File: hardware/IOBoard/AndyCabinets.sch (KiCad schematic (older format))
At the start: 47 parts, among them SW1 Mode_Encoder, SW2 Color_Encoder, U1 74HC14

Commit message: Added faceplate boards
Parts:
- RV1, RV2: footprint Potentiometer_THT:Potentiometer_TT_P0915N -> YonaFootprints:Potentiometer_TT_P0915N_Flush
- U1: footprint (none) -> Package_SO:SOIC-14_3.9x8.7mm_P1.27mm
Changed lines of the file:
@@
 F 0 "RV2" H 3230 3154 50  0000 R CNN
 F 1 "Bright_Pot" H 3230 3245 50  0000 R CNN
-F 2 "Potentiometer_THT:Potentiometer_TT_P0915N" H 3300 3200 50  0001 C CNN
+F 2 "YonaFootprints:Potentiometer_TT_P0915N_Flush" H 3300 3200 50  0001 C CNN
 F 3 "~" H 3300 3200 50  0001 C CNN
 	1    3300 3200
@@
 F 0 "RV1" H 1880 3154 50  0000 R CNN
 F 1 "Speed_Pot" H 1880 3245 50  0000 R CNN
-F 2 "Potentiometer_THT:Potentiometer_TT_P0915N" H 1950 3200 50  0001 C CNN
+F 2 "YonaFootprints:Potentiometer_TT_P0915N_Flush" H 1950 3200 50  0001 C CNN
 F 3 "~" H 1950 3200 50  0001 C CNN
 	1    1950 3200
@@
 F 0 "U1" H 11380 2746 50  0000 L CNN
 F 1 "74HC14" H 11380 2655 50  0000 L CNN
-F 2 "" H 11150 2700 50  0001 C CNN
+F 2 "Package_SO:SOIC-14_3.9x8.7mm_P1.27mm" H 11150 2700 50  0001 C CNN
 F 3 "http://www.ti.com/lit/gpn/sn74HC14" H 11150 2700 50  0001 C CNN
 	7    11150 2700

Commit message: After PCB v2
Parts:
- removed C9: 1uF, Capacitor_SMD:C_0805_2012Metric, symbol Device:C
- C11, C13: value 0.01uF -> 0.1uF
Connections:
- net GPIO32_MODE_BTN: now also U1.12; no longer U1.13
- net GPIO33_MODE_B: now also U1.4; no longer U1.3
- net at C7.1, R7.2: now also U1.3; no longer U1.4
- net at C13.1, R12.1: now also U1.13; no longer U1.12
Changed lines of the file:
@@
-$EndComp
-$Comp
-L power:GNDD #PWR015
-U 1 1 5E283166
-P 6050 3450
-F 0 "#PWR015" H 6050 3200 50  0001 C CNN
-F 1 "GNDD" H 6054 3295 50  0000 C CNN
-F 2 "" H 6050 3450 50  0001 C CNN
-F 3 "" H 6050 3450 50  0001 C CNN
-	1    6050 3450
-	1    0    0    -1
-$EndComp
-$Comp
-L Device:C C9
-U 1 1 5E28316C
-P 6050 3300
-F 0 "C9" H 6165 3346 50  0000 L CNN
-F 1 "1uF" H 6165 3255 50  0000 L CNN
-F 2 "Capacitor_SMD:C_0805_2012Metric" H 6088 3150 50  0001 C CNN
-F 3 "~" H 6050 3300 50  0001 C CNN
-	1    6050 3300
-	1    0    0    -1
-$EndComp
-$Comp
-L AndyCabinets-rescue:+3.3V-ESP32-PoE-ISO_Rev_C #PWR013
-U 1 1 5E28E6C3
-P 6050 3150
-F 0 "#PWR013" H 6050 3000 50  0001 C CNN
-F 1 "+3.3V" H 6065 3278 50  0000 L CNN
-F 2 "" H 6050 3150 60  0000 C CNN
-F 3 "" H 6050 3150 60  0000 C CNN
-	1    6050 3150
-	1    0    0    -1
 $EndComp
 $Comp
@@
 P 8800 2900
 F 0 "C11" H 8915 2946 50  0000 L CNN
-F 1 "0.01uF" H 8915 2855 50  0000 L CNN
+F 1 "0.1uF" H 8915 2855 50  0000 L CNN
 F 2 "Capacitor_SMD:C_0402_1005Metric" H 8838 2750 50  0001 C CNN
 F 3 "~" H 8800 2900 50  0001 C CNN
@@
 $EndComp
 $Comp
-L Device:R R11
-U 1 1 5E44CEB9
-P 8300 5500
-F 0 "R11" H 8150 5550 50  0000 L CNN
-F 1 "10K" H 8100 5450 50  0000 L CNN
-F 2 "Resistor_SMD:R_0402_1005Metric" V 8230 5500 50  0001 C CNN
-F 3 "~" H 8300 5500 50  0001 C CNN
-	1    8300 5500
-	1    0    0    -1
-$EndComp
-$Comp
 L Device:C C13
 U 1 1 5E44CEBF
 P 8800 5800
 F 0 "C13" H 8915 5846 50  0000 L CNN
-F 1 "0.01uF" H 8915 5755 50  0000 L CNN
+F 1 "0.1uF" H 8915 5755 50  0000 L CNN
 F 2 "Capacitor_SMD:C_0402_1005Metric" H 8838 5650 50  0001 C CNN
 F 3 "~" H 8800 5800 50  0001 C CNN
@@
 F 3 "http://www.ti.com/lit/gpn/sn74HC14" H 5750 4800 50  0001 C CNN
 	2    5750 4800
-	1    0    0    -1
+	-1   0    0    1
 $EndComp
 $Comp
@@
 F 3 "http://www.ti.com/lit/gpn/sn74HC14" H 9350 5650 50  0001 C CNN
 	6    9350 5650
-	-1   0    0    1
+	1    0    0    -1
 $EndComp
 Wire Wire Line
@@
 	1    0    0    -1
 $EndComp
+$Comp
+L Device:R R11
+U 1 1 5E44CEB9
+P 8300 5500
+F 0 "R11" H 8100 5550 50  0000 L CNN
+F 1 "10K" H 8100 5450 50  0000 L CNN
+F 2 "Resistor_SMD:R_0402_1005Metric" V 8230 5500 50  0001 C CNN
+F 3 "~" H 8300 5500 50  0001 C CNN
+	1    8300 5500
+	1    0    0    -1
+$EndComp

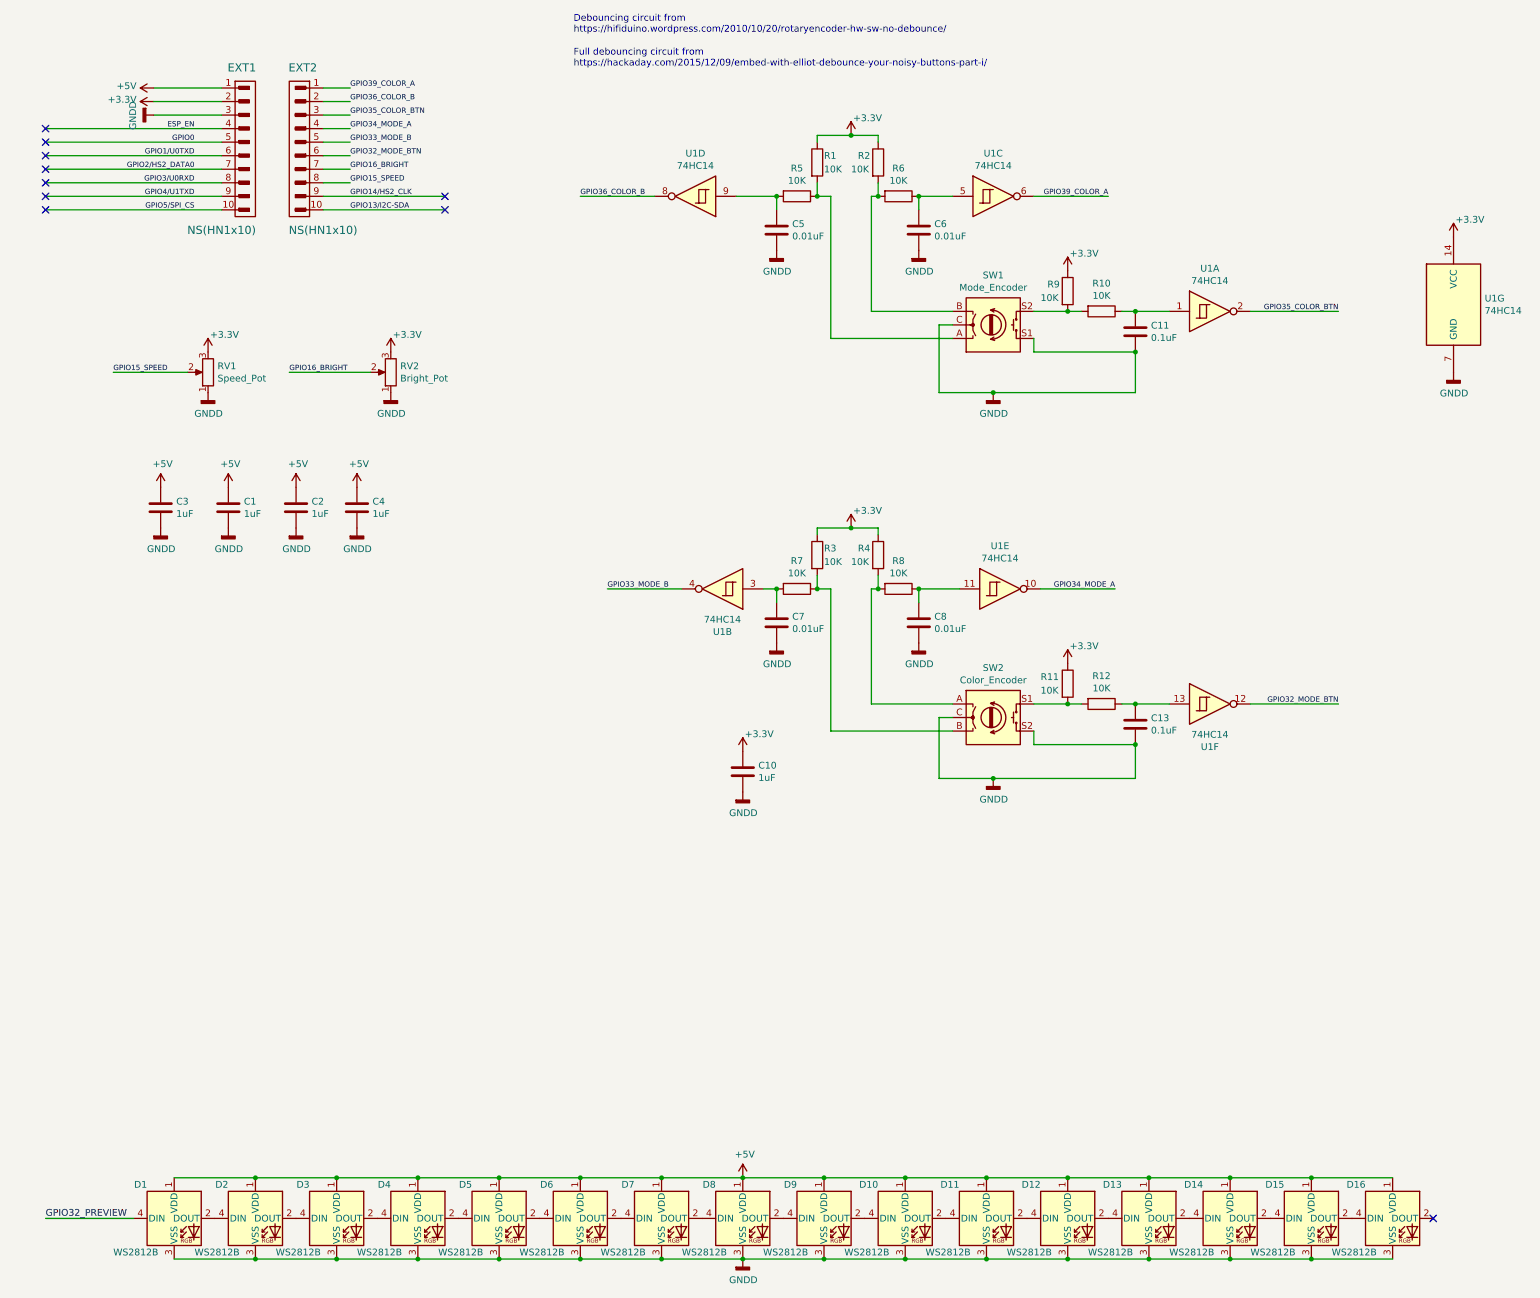
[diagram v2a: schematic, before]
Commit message: Initial working remote version; some minor PCB changes
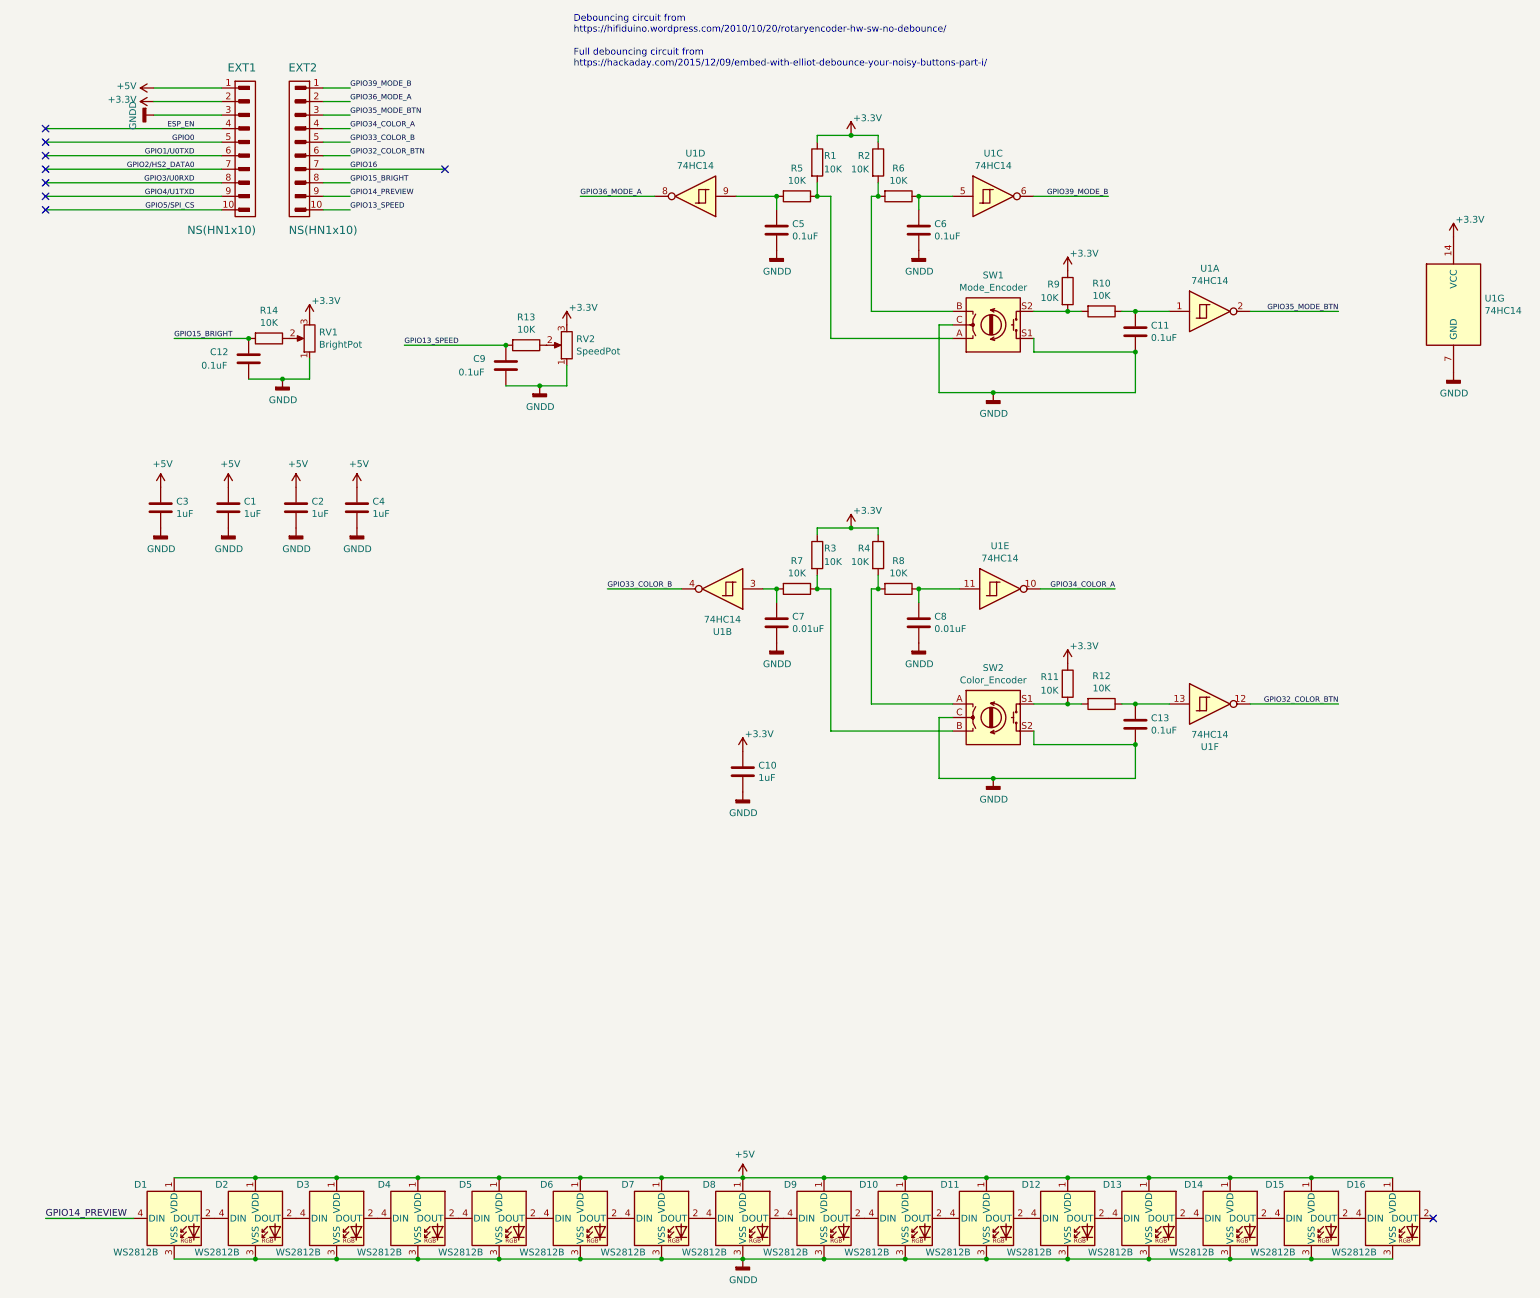
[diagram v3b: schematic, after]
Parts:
- added C12, C9: 0.1uF, Capacitor_SMD:C_0402_1005Metric, symbol Device:C
- added R13, R14: 10K, Resistor_SMD:R_0402_1005Metric, symbol Device:R
- C5, C6: value 0.01uF -> 0.1uF
- RV1: value Speed_Pot -> BrightPot
- RV2: value Bright_Pot -> SpeedPot
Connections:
- net GPIO32_PREVIEW is gone; now on net GPIO14_PREVIEW: D1.4 (DIN)
- net GNDD: now also C12.2, C9.2
- net GPIO13/I2C-SDA renamed GPIO13_SPEED
- net GPIO13_SPEED: now also C9.1, R13.2
- net GPIO14/HS2_CLK renamed GPIO14_PREVIEW
- net GPIO15_SPEED: no longer names the net of RV1.2
- net GPIO15_SPEED: now also R14.1; no longer EXT2.8
- net GPIO16_BRIGHT: no longer names the net of RV2.2
- net GPIO16_BRIGHT: now also R13.1; no longer EXT2.7
- net GPIO32_MODE_BTN renamed GPIO32_COLOR_BTN
- net GPIO33_MODE_B renamed GPIO33_COLOR_B
- net GPIO34_MODE_A renamed GPIO34_COLOR_A
- net GPIO35_COLOR_BTN renamed GPIO35_MODE_BTN
- net GPIO36_COLOR_B renamed GPIO36_MODE_A
- net GPIO39_COLOR_A renamed GPIO39_MODE_B
- new net GPIO15_BRIGHT: C12.1, EXT2.8, R14.2
- new net GPIO16: EXT2.7
- no-connect marks 10 -> 9
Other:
- moved on the sheet: RV1, RV2
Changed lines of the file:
@@
 L Device:R_POT RV2
 U 1 1 5DB1EC9A
-P 3300 3200
-F 0 "RV2" H 3230 3154 50  0000 R CNN
-F 1 "Bright_Pot" H 3230 3245 50  0000 R CNN
-F 2 "YonaFootprints:Potentiometer_TT_P0915N_Flush" H 3300 3200 50  0001 C CNN
-F 3 "~" H 3300 3200 50  0001 C CNN
-	1    3300 3200
+P 4600 3000
+F 0 "RV2" H 4530 2954 50  0000 R CNN
+F 1 "SpeedPot" H 4530 3045 50  0000 R CNN
+F 2 "YonaFootprints:Potentiometer_TT_P0915N_Flush" H 4600 3000 50  0001 C CNN
+F 3 "~" H 4600 3000 50  0001 C CNN
+	1    4600 3000
 	-1   0    0    1
 $EndComp
@@
 L power:GNDD #PWR0104
 U 1 1 5DB22F79
-P 3300 3350
-F 0 "#PWR0104" H 3300 3100 50  0001 C CNN
-F 1 "GNDD" H 3304 3195 50  0000 C CNN
-F 2 "" H 3300 3350 50  0001 C CNN
-F 3 "" H 3300 3350 50  0001 C CNN
-	1    3300 3350
+P 4400 3300
+F 0 "#PWR0104" H 4400 3050 50  0001 C CNN
+F 1 "GNDD" H 4404 3145 50  0000 C CNN
+F 2 "" H 4400 3300 50  0001 C CNN
+F 3 "" H 4400 3300 50  0001 C CNN
+	1    4400 3300
 	1    0    0    -1
 $EndComp
@@
 L Device:R_POT RV1
 U 1 1 5DB2A214
-P 1950 3200
-F 0 "RV1" H 1880 3154 50  0000 R CNN
-F 1 "Speed_Pot" H 1880 3245 50  0000 R CNN
-F 2 "YonaFootprints:Potentiometer_TT_P0915N_Flush" H 1950 3200 50  0001 C CNN
-F 3 "~" H 1950 3200 50  0001 C CNN
-	1    1950 3200
+P 2700 2950
+F 0 "RV1" H 2630 2904 50  0000 R CNN
+F 1 "BrightPot" H 2630 2995 50  0000 R CNN
+F 2 "YonaFootprints:Potentiometer_TT_P0915N_Flush" H 2700 2950 50  0001 C CNN
+F 3 "~" H 2700 2950 50  0001 C CNN
+	1    2700 2950
 	-1   0    0    1
-$EndComp
-$Comp
-L power:GNDD #PWR0106
-U 1 1 5DB2A21A
-P 1950 3350
-F 0 "#PWR0106" H 1950 3100 50  0001 C CNN
-F 1 "GNDD" H 1954 3195 50  0000 C CNN
-F 2 "" H 1950 3350 50  0001 C CNN
-F 3 "" H 1950 3350 50  0001 C CNN
-	1    1950 3350
-	1    0    0    -1
 $EndComp
 $Comp
@@
 $EndComp
 Text Label 750  9450 0    50   ~ 0
-GPIO32_PREVIEW
+GPIO14_PREVIEW
 $Comp
 L LED:WS2812B D2
@@
 Text Label 1850 2000 2    39   ~ 0
 GPIO5/SPI_CS
-Text Label 3000 2000 0    39   ~ 0
-GPIO13/I2C-SDA
 Text Label 3000 1900 0    39   ~ 0
-GPIO14/HS2_CLK
+GPIO14_PREVIEW
 Text Label 3000 1800 0    39   ~ 0
-GPIO15_SPEED
+GPIO15_BRIGHT
 Text Label 3000 1700 0    39   ~ 0
-GPIO16_BRIGHT
+GPIO16
 Text Label 3000 1500 0    39   ~ 0
-GPIO33_MODE_B
+GPIO33_COLOR_B
 Text Label 3000 1400 0    39   ~ 0
-GPIO34_MODE_A
+GPIO34_COLOR_A
 Text Label 3000 1200 0    39   ~ 0
-GPIO36_COLOR_B
+GPIO36_MODE_A
 Text Label 3000 1100 0    39   ~ 0
-GPIO39_COLOR_A
+GPIO39_MODE_B
 $Comp
 L AndyCabinets-rescue:+5V-ESP32-PoE-ISO_Rev_C #PWR0108
@@
 	2050 2000 750  2000
 Wire Wire Line
-	3700 2000 2800 2000
-Wire Wire Line
-	2800 1900 3700 1900
-Wire Wire Line
 	2050 1300 1550 1300
 Wire Wire Line
@@
 	1    0    0    -1
 $EndComp
-NoConn ~ 3700 2000
-NoConn ~ 3700 1900
 NoConn ~ 750  2000
 NoConn ~ 750  1900
@@
 L AndyCabinets-rescue:+3.3V-ESP32-PoE-ISO_Rev_C #PWR0101
 U 1 1 5E0E7FA8
-P 3300 3050
-F 0 "#PWR0101" H 3300 2900 50  0001 C CNN
-F 1 "+3.3V" H 3315 3178 50  0000 L CNN
-F 2 "" H 3300 3050 60  0000 C CNN
-F 3 "" H 3300 3050 60  0000 C CNN
-	1    3300 3050
+P 4600 2850
+F 0 "#PWR0101" H 4600 2700 50  0001 C CNN
+F 1 "+3.3V" H 4615 2978 50  0000 L CNN
+F 2 "" H 4600 2850 60  0000 C CNN
+F 3 "" H 4600 2850 60  0000 C CNN
+	1    4600 2850
 	1    0    0    -1
 $EndComp
@@
 L AndyCabinets-rescue:+3.3V-ESP32-PoE-ISO_Rev_C #PWR0105
 U 1 1 5E0F28C5
-P 1950 3050
-F 0 "#PWR0105" H 1950 2900 50  0001 C CNN
-F 1 "+3.3V" H 1965 3178 50  0000 L CNN
-F 2 "" H 1950 3050 60  0000 C CNN
-F 3 "" H 1950 3050 60  0000 C CNN
-	1    1950 3050
-	1    0    0    -1
-$EndComp
-Wire Wire Line
-	1250 3200 1800 3200
+P 2700 2800
+F 0 "#PWR0105" H 2700 2650 50  0001 C CNN
+F 1 "+3.3V" H 2715 2928 50  0000 L CNN
+F 2 "" H 2700 2800 60  0000 C CNN
+F 3 "" H 2700 2800 60  0000 C CNN
+	1    2700 2800
+	1    0    0    -1
+$EndComp
+Wire Wire Line
+	1700 2950 2250 2950
 Wire Wire Line
 	750  9450 1400 9450
 Wire Wire Line
-	2550 3200 3150 3200
-Wire Wire Line
 	3000 1100 2800 1100
 Wire Wire Line
@@
 	3000 1200 2800 1200
 Wire Wire Line
-	3000 1700 2800 1700
-Wire Wire Line
 	2800 1800 3000 1800
-Text Label 1250 3200 0    39   ~ 0
-GPIO15_SPEED
-Text Label 2550 3200 0    39   ~ 0
-GPIO16_BRIGHT
-Text Label 8600 1900 2    39   ~ 0
-GPIO39_COLOR_A
-Text Label 4700 1900 0    39   ~ 0
-GPIO36_COLOR_B
+Text Label 1700 2950 0    39   ~ 0
+GPIO15_BRIGHT
+Text Label 3400 3000 0    39   ~ 0
+GPIO13_SPEED
 $Comp
 L Device:C C1
@@
 $EndComp
 $Comp
-L Device:C C5
-U 1 1 5E1C5F20
-P 6150 2150
-F 0 "C5" H 6265 2196 50  0000 L CNN
-F 1 "0.01uF" H 6265 2105 50  0000 L CNN
-F 2 "Capacitor_SMD:C_0402_1005Metric" H 6188 2000 50  0001 C CNN
-F 3 "~" H 6150 2150 50  0001 C CNN
-	1    6150 2150
-	1    0    0    -1
-$EndComp
-$Comp
 L power:GNDD #PWR0102
 U 1 1 5E1C6A2D
@@
 P 7200 2150
 F 0 "C6" H 7315 2196 50  0000 L CNN
-F 1 "0.01uF" H 7315 2105 50  0000 L CNN
+F 1 "0.1uF" H 7315 2105 50  0000 L CNN
 F 2 "Capacitor_SMD:C_0402_1005Metric" H 7238 2000 50  0001 C CNN
 F 3 "~" H 7200 2150 50  0001 C CNN
@@
 $EndComp
 Text Label 8650 4800 2    39   ~ 0
-GPIO34_MODE_A
+GPIO34_COLOR_A
 Text Notes 4650 700  0    50   ~ 0
 Debouncing circuit from \nhttps://hifiduino.wordpress.com/2010/10/20/rotaryencoder-hw-sw-no-debounce/
@@
 	3000 1300 2800 1300
 Text Label 3000 1600 0    39   ~ 0
-GPIO32_MODE_BTN
+GPIO32_COLOR_BTN
 Text Label 3000 1300 0    39   ~ 0
-GPIO35_COLOR_BTN
+GPIO35_MODE_BTN
 $Comp
 L power:+5V #PWR04
@@
 	7450 5750 7350 5750
 Text Label 10300 2750 2    39   ~ 0
-GPIO35_COLOR_BTN
+GPIO35_MODE_BTN
 Text Label 10300 5650 2    39   ~ 0
-GPIO32_MODE_BTN
+GPIO32_COLOR_BTN
 $Comp
 L power:GNDD #PWR0103
@@
 Connection ~ 8800 3050
 Text Label 4900 4800 0    39   ~ 0
-GPIO33_MODE_B
+GPIO33_COLOR_B
 $Comp
 L 74xx:74HC14 U1
@@
 $Comp
 L 74xx:74HC14 U1
-U 3 1 5E46D9F8
-P 7750 1900
-F 0 "U1" H 7750 2217 50  0000 C CNN
-F 1 "74HC14" H 7750 2126 50  0000 C CNN
-F 2 "Package_SO:SOIC-14_3.9x8.7mm_P1.27mm" H 7750 1900 50  0001 C CNN
-F 3 "http://www.ti.com/lit/gpn/sn74HC14" H 7750 1900 50  0001 C CNN
-	3    7750 1900
-	1    0    0    -1
-$EndComp
-$Comp
-L 74xx:74HC14 U1
 U 4 1 5E46F5E2
 P 5550 1900
@@
 	1    0    0    -1
 $EndComp
+$Comp
+L 74xx:74HC14 U1
+U 3 1 5E46D9F8
+P 7750 1900
+F 0 "U1" H 7750 2217 50  0000 C CNN
+F 1 "74HC14" H 7750 2126 50  0000 C CNN
+F 2 "Package_SO:SOIC-14_3.9x8.7mm_P1.27mm" H 7750 1900 50  0001 C CNN
+F 3 "http://www.ti.com/lit/gpn/sn74HC14" H 7750 1900 50  0001 C CNN
+	3    7750 1900
+	1    0    0    -1
+$EndComp
+$Comp
+L Device:R R13
+U 1 1 5E210549
+P 4300 3000
+F 0 "R13" V 4093 3000 50  0000 C CNN
+F 1 "10K" V 4184 3000 50  0000 C CNN
+F 2 "Resistor_SMD:R_0402_1005Metric" V 4230 3000 50  0001 C CNN
+F 3 "~" H 4300 3000 50  0001 C CNN
+	1    4300 3000
+	0    1    1    0
+$EndComp
+$Comp
+L Device:C C5
+U 1 1 5E1C5F20
+P 6150 2150
+F 0 "C5" H 6265 2196 50  0000 L CNN
+F 1 "0.1uF" H 6265 2105 50  0000 L CNN
+F 2 "Capacitor_SMD:C_0402_1005Metric" H 6188 2000 50  0001 C CNN
+F 3 "~" H 6150 2150 50  0001 C CNN
+	1    6150 2150
+	1    0    0    -1
+$EndComp
+$Comp
+L Device:C C9
+U 1 1 5E217494
+P 4150 3150
+F 0 "C9" H 4000 3200 50  0000 R CNN
+F 1 "0.1uF" H 3800 3100 50  0000 L CNN
+F 2 "Capacitor_SMD:C_0402_1005Metric" H 4188 3000 50  0001 C CNN
+F 3 "~" H 4150 3150 50  0001 C CNN
+	1    4150 3150
+	1    0    0    -1
+$EndComp
+Wire Wire Line
+	4600 3150 4600 3300
+Wire Wire Line
+	4600 3300 4400 3300
+Connection ~ 4400 3300
+Wire Wire Line
+	4400 3300 4150 3300
+Wire Wire Line
+	3400 3000 4150 3000
+Connection ~ 4150 3000
+$Comp
+L power:GNDD #PWR013
+U 1 1 5E226259
+P 2500 3250
+F 0 "#PWR013" H 2500 3000 50  0001 C CNN
+F 1 "GNDD" H 2504 3095 50  0000 C CNN
+F 2 "" H 2500 3250 50  0001 C CNN
+F 3 "" H 2500 3250 50  0001 C CNN
+	1    2500 3250
+	1    0    0    -1
+$EndComp
+$Comp
+L Device:R R14
+U 1 1 5E22625F
+P 2400 2950
+F 0 "R14" V 2193 2950 50  0000 C CNN
+F 1 "10K" V 2284 2950 50  0000 C CNN
+F 2 "Resistor_SMD:R_0402_1005Metric" V 2330 2950 50  0001 C CNN
+F 3 "~" H 2400 2950 50  0001 C CNN
+	1    2400 2950
+	0    1    1    0
+$EndComp
+$Comp
+L Device:C C12
+U 1 1 5E226265
+P 2250 3100
+F 0 "C12" H 2100 3150 50  0000 R CNN
+F 1 "0.1uF" H 1900 3050 50  0000 L CNN
+F 2 "Capacitor_SMD:C_0402_1005Metric" H 2288 2950 50  0001 C CNN
+F 3 "~" H 2250 3100 50  0001 C CNN
+	1    2250 3100
+	1    0    0    -1
+$EndComp
+Wire Wire Line
+	2700 3250 2500 3250
+Connection ~ 2500 3250
+Wire Wire Line
+	2500 3250 2250 3250
+Connection ~ 2250 2950
+Wire Wire Line
+	2700 3100 2700 3250
+Wire Wire Line
+	2800 1700 3700 1700
+NoConn ~ 3700 1700
+Wire Wire Line
+	3000 1900 2800 1900
+Wire Wire Line
+	2800 2000 3000 2000
+Text Label 3000 2000 0    39   ~ 0
+GPIO13_SPEED
+Text Label 8600 1900 2    39   ~ 0
+GPIO39_MODE_B
+Text Label 4700 1900 0    39   ~ 0
+GPIO36_MODE_A
 $EndSCHEMATC
